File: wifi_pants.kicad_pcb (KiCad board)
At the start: 2 copper layers, 65 x 30 mm, 135 parts, among them P1 CONN_02X20, P2 POWER / UART, P3 JST PH POWER IN, U1 ESP-12E, U2 TPS6123x

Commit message: v3 complete layout
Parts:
- removed the REF** at (74.4, 99.7)
- removed the REF** at (73.6, 105.3)
- removed the REF** at (74.4, 109.4)
- removed the REF** at (71.8, 90.7)
- removed the REF** at (75.8, 102.1)
- removed the REF**101 at (120.3, 85.8)
- removed REF**31, REF**41, REF**51, REF**61, REF**71, REF**81, REF**91: VIA_0.40mm, wifi_pants:VIA_0.40mm
- added REF**1: VIA_0.40mm, wifi_pants:VIA_0.40mm, F.Cu at (86.3, 106.5)
- added REF**6: VIA_0.40mm, wifi_pants:VIA_0.40mm, F.Cu at (83.3, 111.0)
- added REF**6: VIA_0.40mm, wifi_pants:VIA_0.40mm, F.Cu at (74.9, 109.7)
- moved REF**21 20.6 mm to (100.0, 88.5)
- moved REF**11 10.6 mm to (84.8, 88.5)
- moved REF** 1.70 mm to (79.5, 101.1)
- moved REF** 0.92 mm to (78.3, 105.9)
- moved REF** 0.87 mm to (82.5, 108.7)
- moved REF** 0.68 mm to (70.9, 104.9)
- moved REF** 0.61 mm to (76.7, 98.0)
- moved REF** 0.52 mm to (74.3, 95.5)
- moved REF** 0.40 mm to (75.2, 104.9)
- moved REF**1 0.28 mm to (103.4, 113.0)
- moved REF**6 0.27 mm to (103.1, 110.2)
- moved REF** 0.25 mm to (73.4, 113.0)
- moved REF**1 0.23 mm to (83.8, 113.1)
- moved REF**1 0.12 mm to (79.3, 113.1)
- renumbered C4 to C2, C5 to C3, C6 to C4, C2 to C5, C3 to C6
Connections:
- net /PSU_SHDN renamed /SHDN
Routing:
- net PI_UART0_TXD: track 82.5 -> 79.4 mm
- net +3V3: track 26.7 -> 24.1 mm
- net PI_UART0_RXD: track 75.8 -> 78.2 mm
- net ID_SD: track 45.4 -> 47.3 mm
- net /SHDN: track 25.5 -> 27.1 mm
- net +5V: track 71.7 -> 70.4 mm
- net Net-(JP3-Pad1): track 4.55 -> 5.46 mm
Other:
- board text added: "/SHDN isolation"
- board text added: "github.com/ al177/ wifi_pants"
- board text added: "hac.io/ project/ 8678"
- board text removed: "/PWR_SHDN isolation"
- board text removed: "github.com/al177 /wifi_pants"

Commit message: Fab files for v3
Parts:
- added REF**: Symbol_OSHW-Logo_SilkScreen, Symbols:Symbol_OSHW-Logo_SilkScreen, F.Cu at (94.7, 95.0)
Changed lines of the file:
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@@
 (kicad_pcb (version 4) (host pcbnew 4.0.0-stable)
   (general
-    (links 161)
+    (links 0)
     (no_connects 0)
     (area 64.924999 84.924999 130.075001 115.075001)
@@
     (tracks 390)
     (zones 0)
-    (modules 125)
+    (modules 126)
     (nets 59)
   )
@@
       (usegerberextensions true)
       (excludeedgelayer true)
-      (linewidth 0.150000)
+      (linewidth 0.100000)
       (plotframeref false)
       (viasonmask false)
@@
     (descr "Through hole socket strip")
     (tags "socket strip")
-    (fp_text reference P1 (at -24.13 6.37) (layer B.SilkS)
+    (fp_text reference P1 (at -24.65 4) (layer B.SilkS)
       (effects (font (size 1 1) (thickness 0.15)) (justify mirror))
     )
@@
     )
   )
+  (module Symbols:Symbol_OSHW-Logo_SilkScreen (layer F.Cu)
+    (at 94.7 94.95 90)
+    (descr "Symbol, OSHW-Logo, Silk Screen,")
+    (tags "Symbol, OSHW-Logo, Silk Screen,")
+    (fp_text reference REF** (at 0.09906 -4.38912 90) (layer F.SilkS) hide
+      (effects (font (size 1 1) (thickness 0.15)))
+    )
+    (fp_text value Symbol_OSHW-Logo_SilkScreen (at 0.30988 6.56082 90) (layer F.Fab)
+      (effects (font (size 1 1) (thickness 0.15)))
+    )
+    (fp_line (start 1.66878 2.68986) (end 2.02946 4.16052) (layer F.SilkS) (width 0.15))
+    (fp_line (start 2.02946 4.16052) (end 2.30886 3.0988) (layer F.SilkS) (width 0.15))
+    (fp_line (start 2.30886 3.0988) (end 2.61874 4.17068) (layer F.SilkS) (width 0.15))
+    (fp_line (start 2.61874 4.17068) (end 2.9591 2.72034) (layer F.SilkS) (width 0.15))
+    (fp_line (start 0.24892 3.38074) (end 1.03886 3.37058) (layer F.SilkS) (width 0.15))
+    (fp_line (start 1.03886 3.37058) (end 1.04902 3.38074) (layer F.SilkS) (width 0.15))
+    (fp_line (start 1.04902 3.38074) (end 1.04902 3.37058) (layer F.SilkS) (width 0.15))
+    (fp_line (start 1.08966 2.65938) (end 1.08966 4.20116) (layer F.SilkS) (width 0.15))
+    (fp_line (start 0.20066 2.64922) (end 0.20066 4.21894) (layer F.SilkS) (width 0.15))
+    (fp_line (start 0.20066 4.21894) (end 0.21082 4.20878) (layer F.SilkS) (width 0.15))
+    (fp_line (start -0.35052 2.75082) (end -0.70104 2.66954) (layer F.SilkS) (width 0.15))
+    (fp_line (start -0.70104 2.66954) (end -1.02108 2.65938) (layer F.SilkS) (width 0.15))
+    (fp_line (start -1.02108 2.65938) (end -1.25984 2.86004) (layer F.SilkS) (width 0.15))
+    (fp_line (start -1.25984 2.86004) (end -1.29032 3.12928) (layer F.SilkS) (width 0.15))
+    (fp_line (start -1.29032 3.12928) (end -1.04902 3.37058) (layer F.SilkS) (width 0.15))
+    (fp_line (start -1.04902 3.37058) (end -0.6604 3.50012) (layer F.SilkS) (width 0.15))
+    (fp_line (start -0.6604 3.50012) (end -0.48006 3.66014) (layer F.SilkS) (width 0.15))
+    (fp_line (start -0.48006 3.66014) (end -0.43942 3.95986) (layer F.SilkS) (width 0.15))
+    (fp_line (start -0.43942 3.95986) (end -0.67056 4.18084) (layer F.SilkS) (width 0.15))
+    (fp_line (start -0.67056 4.18084) (end -0.9906 4.20878) (layer F.SilkS) (width 0.15))
+    (fp_line (start -0.9906 4.20878) (end -1.34112 4.09956) (layer F.SilkS) (width 0.15))
+    (fp_line (start -2.37998 2.64922) (end -2.6289 2.66954) (layer F.SilkS) (width 0.15))
+    (fp_line (start -2.6289 2.66954) (end -2.8702 2.91084) (layer F.SilkS) (width 0.15))
+    (fp_line (start -2.8702 2.91084) (end -2.9591 3.40106) (layer F.SilkS) (width 0.15))
+    (fp_line (start -2.9591 3.40106) (end -2.93116 3.74904) (layer F.SilkS) (width 0.15))
+    (fp_line (start -2.93116 3.74904) (end -2.7305 4.06908) (layer F.SilkS) (width 0.15))
+    (fp_line (start -2.7305 4.06908) (end -2.47904 4.191) (layer F.SilkS) (width 0.15))
+    (fp_line (start -2.47904 4.191) (end -2.16916 4.11988) (layer F.SilkS) (width 0.15))
+    (fp_line (start -2.16916 4.11988) (end -1.95072 3.93954) (layer F.SilkS) (width 0.15))
+    (fp_line (start -1.95072 3.93954) (end -1.8796 3.4798) (layer F.SilkS) (width 0.15))
+    (fp_line (start -1.8796 3.4798) (end -1.9304 3.07086) (layer F.SilkS) (width 0.15))
+    (fp_line (start -1.9304 3.07086) (end -2.03962 2.78892) (layer F.SilkS) (width 0.15))
+    (fp_line (start -2.03962 2.78892) (end -2.4003 2.65938) (layer F.SilkS) (width 0.15))
+    (fp_line (start -1.78054 0.92964) (end -2.03962 1.49098) (layer F.SilkS) (width 0.15))
+    (fp_line (start -2.03962 1.49098) (end -1.50114 2.00914) (layer F.SilkS) (width 0.15))
+    (fp_line (start -1.50114 2.00914) (end -0.98044 1.7399) (layer F.SilkS) (width 0.15))
+    (fp_line (start -0.98044 1.7399) (end -0.70104 1.89992) (layer F.SilkS) (width 0.15))
+    (fp_line (start 0.73914 1.8796) (end 1.06934 1.6891) (layer F.SilkS) (width 0.15))
+    (fp_line (start 1.06934 1.6891) (end 1.50876 2.0193) (layer F.SilkS) (width 0.15))
+    (fp_line (start 1.50876 2.0193) (end 1.9812 1.52908) (layer F.SilkS) (width 0.15))
+    (fp_line (start 1.9812 1.52908) (end 1.69926 1.04902) (layer F.SilkS) (width 0.15))
+    (fp_line (start 1.69926 1.04902) (end 1.88976 0.57912) (layer F.SilkS) (width 0.15))
+    (fp_line (start 1.88976 0.57912) (end 2.49936 0.39116) (layer F.SilkS) (width 0.15))
+    (fp_line (start 2.49936 0.39116) (end 2.49936 -0.28956) (layer F.SilkS) (width 0.15))
+    (fp_line (start 2.49936 -0.28956) (end 1.94056 -0.42926) (layer F.SilkS) (width 0.15))
+    (fp_line (start 1.94056 -0.42926) (end 1.7399 -1.00076) (layer F.SilkS) (width 0.15))
+    (fp_line (start 1.7399 -1.00076) (end 2.00914 -1.47066) (layer F.SilkS) (width 0.15))
+    (fp_line (start 2.00914 -1.47066) (end 1.53924 -1.9812) (layer F.SilkS) (width 0.15))
+    (fp_line (start 1.53924 -1.9812) (end 1.02108 -1.71958) (layer F.SilkS) (width 0.15))
+    (fp_line (start 1.02108 -1.71958) (end 0.55118 -1.92024) (layer F.SilkS) (width 0.15))
+    (fp_line (start 0.55118 -1.92024) (end 0.381 -2.46126) (layer F.SilkS) (width 0.15))
+    (fp_line (start 0.381 -2.46126) (end -0.30988 -2.47904) (layer F.SilkS) (width 0.15))
+    (fp_line (start -0.30988 -2.47904) (end -0.5207 -1.9304) (layer F.SilkS) (width 0.15))
+    (fp_line (start -0.5207 -1.9304) (end -0.9398 -1.76022) (layer F.SilkS) (width 0.15))
+    (fp_line (start -0.9398 -1.76022) (end -1.49098 -2.02946) (layer F.SilkS) (width 0.15))
+    (fp_line (start -1.49098 -2.02946) (end -2.00914 -1.50114) (layer F.SilkS) (width 0.15))
+    (fp_line (start -2.00914 -1.50114) (end -1.76022 -0.96012) (layer F.SilkS) (width 0.15))
+    (fp_line (start -1.76022 -0.96012) (end -1.9304 -0.48006) (layer F.SilkS) (width 0.15))
+    (fp_line (start -1.9304 -0.48006) (end -2.47904 -0.381) (layer F.SilkS) (width 0.15))
+    (fp_line (start -2.47904 -0.381) (end -2.4892 0.32004) (layer F.SilkS) (width 0.15))
+    (fp_line (start -2.4892 0.32004) (end -1.9304 0.5207) (layer F.SilkS) (width 0.15))
+    (fp_line (start -1.9304 0.5207) (end -1.7907 0.91948) (layer F.SilkS) (width 0.15))
+    (fp_line (start 0.35052 0.89916) (end 0.65024 0.7493) (layer F.SilkS) (width 0.15))
+    (fp_line (start 0.65024 0.7493) (end 0.8509 0.55118) (layer F.SilkS) (width 0.15))
+    (fp_line (start 0.8509 0.55118) (end 1.00076 0.14986) (layer F.SilkS) (width 0.15))
+    (fp_line (start 1.00076 0.14986) (end 1.00076 -0.24892) (layer F.SilkS) (width 0.15))
+    (fp_line (start 1.00076 -0.24892) (end 0.8509 -0.59944) (layer F.SilkS) (width 0.15))
+    (fp_line (start 0.8509 -0.59944) (end 0.39878 -0.94996) (layer F.SilkS) (width 0.15))
+    (fp_line (start 0.39878 -0.94996) (end -0.0508 -1.00076) (layer F.SilkS) (width 0.15))
+    (fp_line (start -0.0508 -1.00076) (end -0.44958 -0.89916) (layer F.SilkS) (width 0.15))
+    (fp_line (start -0.44958 -0.89916) (end -0.8509 -0.55118) (layer F.SilkS) (width 0.15))
+    (fp_line (start -0.8509 -0.55118) (end -1.00076 -0.09906) (layer F.SilkS) (width 0.15))
+    (fp_line (start -1.00076 -0.09906) (end -0.94996 0.39878) (layer F.SilkS) (width 0.15))
+    (fp_line (start -0.94996 0.39878) (end -0.70104 0.70104) (layer F.SilkS) (width 0.15))
+    (fp_line (start -0.70104 0.70104) (end -0.35052 0.89916) (layer F.SilkS) (width 0.15))
+    (fp_line (start -0.35052 0.89916) (end -0.70104 1.89992) (layer F.SilkS) (width 0.15))
+    (fp_line (start 0.35052 0.89916) (end 0.7493 1.89992) (layer F.SilkS) (width 0.15))
+  )
   (gr_circle (center 119.089317 89.766717) (end 120.227237 90.117237) (layer B.SilkS) (width 0.3))

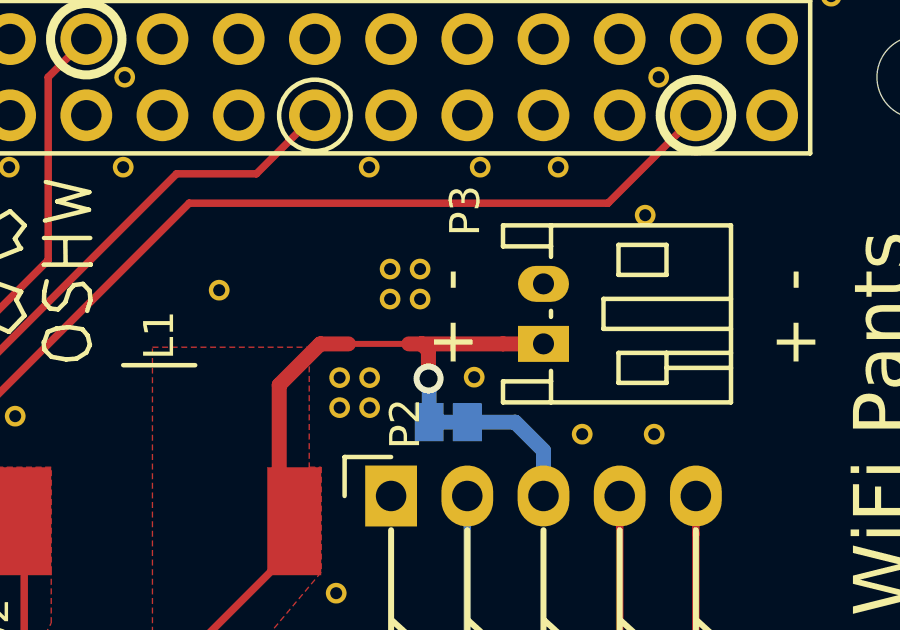
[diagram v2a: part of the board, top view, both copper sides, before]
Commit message: Fix some part#s in the schematic, clean up the back side silk for the JST connector
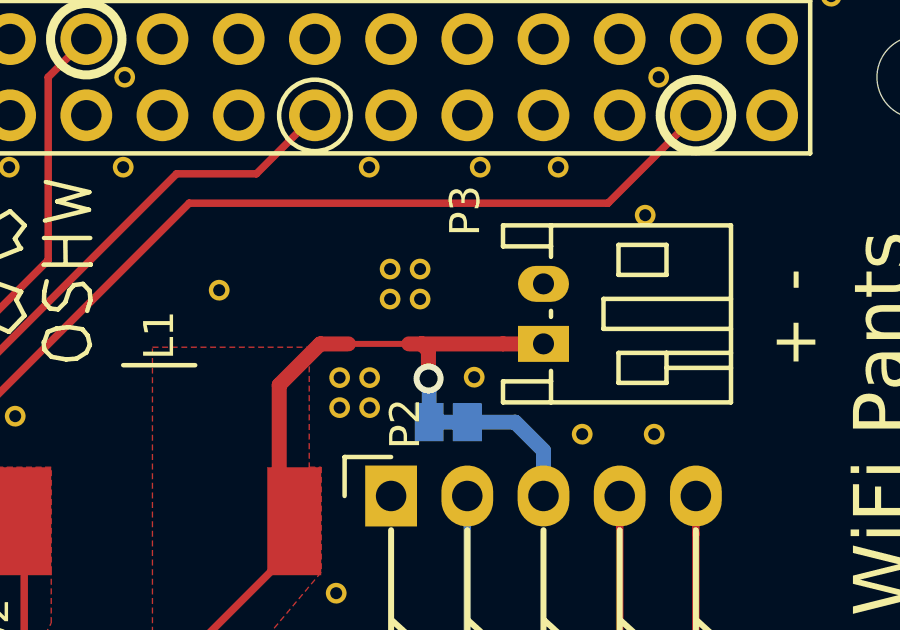
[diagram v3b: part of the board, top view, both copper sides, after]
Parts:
- R7: value 47K -> 22K
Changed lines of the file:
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@@
 (kicad_pcb (version 4) (host pcbnew 4.0.0-stable)
   (general
-    (links 0)
+    (links 161)
     (no_connects 0)
     (area 64.924999 84.924999 130.075001 115.075001)
     (thickness 1.6)
-    (drawings 97)
+    (drawings 94)
     (tracks 390)
     (zones 0)
@@
       (effects (font (size 0.762 0.762) (thickness 0.1524)))
     )
-    (fp_text value 47K (at 0 0) (layer F.SilkS) hide
+    (fp_text value 22K (at 0 0) (layer F.SilkS) hide
       (effects (font (size 0.762 0.762) (thickness 0.1524)))
     )
@@
     (descr "Through hole socket strip")
     (tags "socket strip")
-    (fp_text reference P1 (at -24.65 4) (layer B.SilkS)
+    (fp_text reference P1 (at -24.65 4 90) (layer B.SilkS)
       (effects (font (size 1 1) (thickness 0.15)) (justify mirror))
     )
@@
     (fp_line (start 0.35052 0.89916) (end 0.7493 1.89992) (layer F.SilkS) (width 0.15))
   )
+  (gr_line (start 109.3 99.302872) (end 108.8 99.302872) (layer B.SilkS) (width 0.2))
+  (gr_line (start 115.627272 99.302872) (end 112.37272 99.302872) (layer B.SilkS) (width 0.2))
+  (gr_line (start 108.007272 93.460872) (end 115.627272 93.460872) (layer B.SilkS) (width 0.2))
+  (gr_line (start 115.627272 98.667872) (end 114.103272 98.667872) (layer B.SilkS) (width 0.2))
+  (gr_line (start 115.627272 99.302872) (end 115.627272 98.667872) (layer B.SilkS) (width 0.2))
+  (gr_line (start 115.627272 94.095872) (end 114.103272 94.095872) (layer B.SilkS) (width 0.2))
+  (gr_line (start 115.627272 93.460872) (end 115.627272 94.095872) (layer B.SilkS) (width 0.2))
   (gr_circle (center 119.089317 89.766717) (end 120.227237 90.117237) (layer B.SilkS) (width 0.3))
   (gr_circle (center 106.388477 89.77376) (end 107.526397 90.12428) (layer B.SilkS) (width 0.15))
@@
   )
   (gr_line (start 78.486 97.292) (end 79.666 98.552) (layer B.SilkS) (width 0.2))
-  (gr_line (start 107.99 97.4) (end 109.17 98.66) (layer B.SilkS) (width 0.2))
+  (gr_line (start 106.436 101.51) (end 107.696 100.33) (layer B.SilkS) (width 0.2))
   (gr_line (start 119.09 113.12) (end 119.09 103.6) (layer B.SilkS) (width 0.2))
   (gr_line (start 116.55 113.12) (end 116.55 103.6) (layer B.SilkS) (width 0.2))
@@
     (effects (font (size 1 1) (thickness 0.15)) (justify mirror))
   )
-  (gr_text "PWR_IN\nisolation" (at 106.172 94.742 90) (layer B.SilkS)
+  (gr_text "PWR_IN\nisolation" (at 104.74 103.41 90) (layer B.SilkS)
     (effects (font (size 1 1) (thickness 0.15)) (justify mirror))
   )
-  (gr_text + (at 110.998 97.409 180) (layer B.SilkS)
+  (gr_text + (at 105.918 97.409 180) (layer B.SilkS)
     (effects (font (size 1.5 1.5) (thickness 0.3)) (justify mirror))
   )
-  (gr_text - (at 111.125 95.377 270) (layer B.SilkS)
-    (effects (font (size 1.5 1.5) (thickness 0.3)) (justify mirror))
-  )
-  (gr_text + (at 122.428 97.409 180) (layer B.SilkS)
-    (effects (font (size 1.5 1.5) (thickness 0.3)) (justify mirror))
-  )
-  (gr_text - (at 122.555 95.377 270) (layer B.SilkS)
+  (gr_text - (at 106.045 95.377 270) (layer B.SilkS)
     (effects (font (size 1.5 1.5) (thickness 0.3)) (justify mirror))
   )
@@
     (effects (font (size 1.5 1.5) (thickness 0.3)))
   )
-  (gr_line (start 114.173 96.266) (end 114.173 96.52) (layer B.SilkS) (width 0.2))
-  (gr_line (start 114.173 94.107) (end 114.173 94.488) (layer B.SilkS) (width 0.2))
-  (gr_line (start 112.649 94.107) (end 114.173 94.107) (layer B.SilkS) (width 0.2))
-  (gr_line (start 112.649 93.472) (end 112.649 94.107) (layer B.SilkS) (width 0.2))
-  (gr_line (start 114.173 98.679) (end 114.173 98.298) (layer B.SilkS) (width 0.2))
-  (gr_line (start 112.649 98.679) (end 114.173 98.679) (layer B.SilkS) (width 0.2))
-  (gr_line (start 112.649 99.314) (end 112.649 98.679) (layer B.SilkS) (width 0.2))
-  (gr_line (start 120.269 99.314) (end 112.649 99.314) (layer B.SilkS) (width 0.2))
-  (gr_line (start 120.269 93.472) (end 120.269 99.314) (layer B.SilkS) (width 0.2))
-  (gr_line (start 112.649 93.472) (end 120.269 93.472) (layer B.SilkS) (width 0.2))
-  (gr_text - (at 110.871 95.25 90) (layer F.SilkS)
-    (effects (font (size 1.5 1.5) (thickness 0.3)))
-  )
-  (gr_text + (at 110.998 97.282) (layer F.SilkS)
-    (effects (font (size 1.5 1.5) (thickness 0.3)))
-  )
+  (gr_line (start 114.103272 96.404) (end 114.103272 96.15) (layer B.SilkS) (width 0.2))
+  (gr_line (start 114.103272 98.667872) (end 114.103272 98.286872) (layer B.SilkS) (width 0.2))
+  (gr_line (start 114.103272 94.095872) (end 114.103272 94.476872) (layer B.SilkS) (width 0.2))
+  (gr_line (start 108.007272 98.002872) (end 108.007272 93.460872) (layer B.SilkS) (width 0.2))
   (gr_line (start 108.93 113.12) (end 108.93 103.6) (layer B.SilkS) (width 0.2))
   (gr_text TXD (at 117.89 110.34 90) (layer B.SilkS)
@@
     (min_thickness 0.254)
     (keepout (tracks allowed) (vias allowed) (copperpour not_allowed))
-    (fill yes (arc_segments 16) (thermal_gap 0.508) (thermal_bridge_width 0.508))
+    (fill (arc_segments 16) (thermal_gap 0.508) (thermal_bridge_width 0.508))
     (polygon
       (pts
